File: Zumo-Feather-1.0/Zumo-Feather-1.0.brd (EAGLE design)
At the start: 68.6 x 53.3 mm, 2 parts, among them U1 ARDUINOR3-DIMENSION

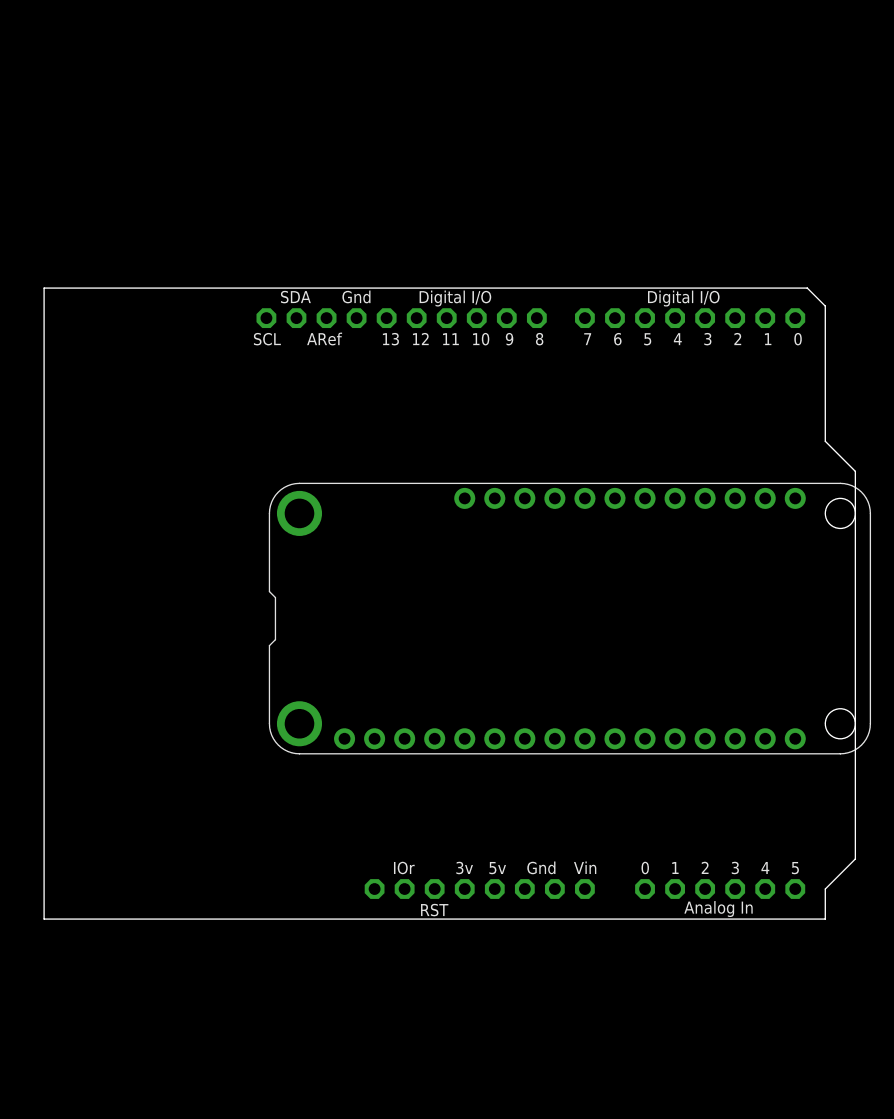
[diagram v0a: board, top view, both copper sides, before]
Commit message: Added CAD and worked on Feather-Zumo Interface board
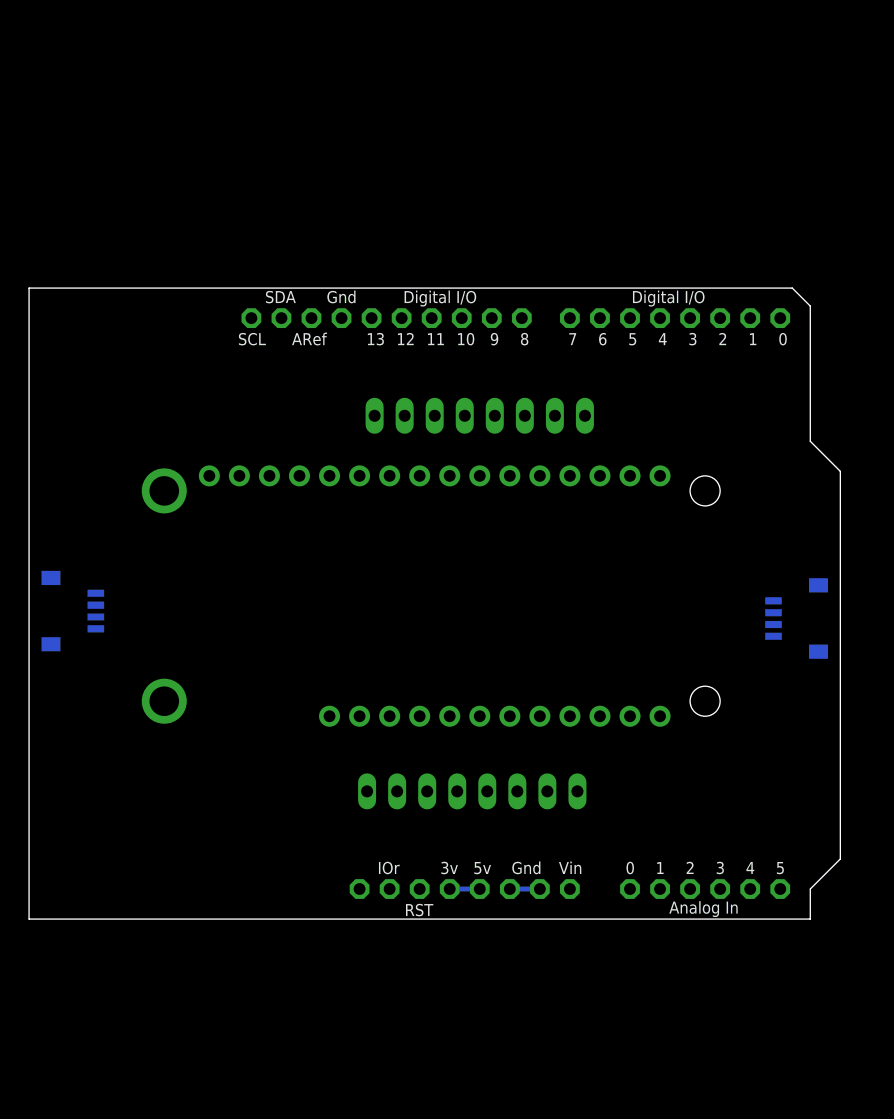
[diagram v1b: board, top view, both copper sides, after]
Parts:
- added J1, J2: (no value), AIMRL:JST_SH_4X1
- added JP1, JP2: (no value), pinhead:1X08
- MS1: value FEATHERWING_NODIM -> BRD-FEATHERWING_NODIM; device adafruit:FEATHERWING_DIM -> AIMRL:FEATHERWING_DIM
- U1: value ARDUINOR3-DIMENSION -> BRD-ARDUINOR3-DIMENSION; device adafruit:ARDUINOR3 -> AIMRL:ARDUINOR3
- moved MS1 27.3 mm to (8.89, 38.7), flipped to the bottom, turned to 180 degrees
- moved U1 1.27 mm to (0.00, 0.00)
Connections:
- net GPIOA0 renamed A0
- net GPIOA2 renamed A2
- net GPIOA3 renamed A3
- net GPIOA4 renamed A4
- net GPIOA5 renamed A5
- net GPIOMISO renamed MISO
- net GPIOMOSI renamed MOSI
- net GPIORX renamed RX
- net GPIOSCK renamed SCK
- net GPIOTX renamed TX
- net USB renamed VUSB
- removed net 5V: U1.5V
- removed net GND1: U1.GND1
- removed net GND2: U1.GND2
- removed net GPIO10: MS1.22
- removed net GPIO11: MS1.23
- removed net GPIO12: MS1.24
- removed net GPIO13: MS1.25
- removed net GPIO5: MS1.19
- removed net GPIO6: MS1.20
- removed net GPIO9: MS1.21
- removed net GPIOA1: MS1.6
- removed net GPIOSCL: MS1.18
- removed net GPIOSDA: MS1.17
- removed net NC: MS1.16
- new net A1: MS1.6, U1.A1
- new net BUZZER: MS1.20, U1.D6
- new net M1DIR: MS1.19, U1.D7
- new net M1PWM: MS1.21, U1.D9
- new net M2DIR: MS1.23, U1.D8
- new net M2PWM: MS1.22, U1.D10
- new net N$1: J1.1, J2.1
- new net N$10: JP2.6
- new net N$11: JP2.7
- new net N$12: JP2.8
- new net N$13: JP1.1
- new net N$14: JP1.2
- new net N$15: JP1.3
- new net N$16: JP1.4
- new net N$17: JP1.5
- new net N$18: JP1.6
- new net N$19: JP1.7
- new net N$2: J1.2, J2.2
- new net N$20: JP1.8
- new net N$3: J1.3, J2.3
- new net N$4: J1.4, J2.4
- new net N$5: JP2.1
- new net N$6: JP2.2
- new net N$7: JP2.3
- new net N$8: JP2.4
- new net N$9: JP2.5
- new net SCL: MS1.18, U1.SCL
- new net SDA: MS1.17, U1.SDA
- new net USER_SW: MS1.24, U1.D12
- new net YELLOW_LED: MS1.25, U1.D13
- net !RESET: now also U1.RESET
- net 3V: now also U1.5V
- net AREF: now also U1.AREF
- net GND: now also U1.GND1, U1.GND2
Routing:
- net GND: track 0.00 -> 2.54 mm
- net 3V: track 0.00 -> 2.54 mm

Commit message: Worked on Zumo board
Swapped pinout around a bunch to make layout easier. Realized power is provided by a 7.5V boost converter, which is not ideal. I will need to jumper VBATT directly from the Zumo Shield or bypass the boost converter.
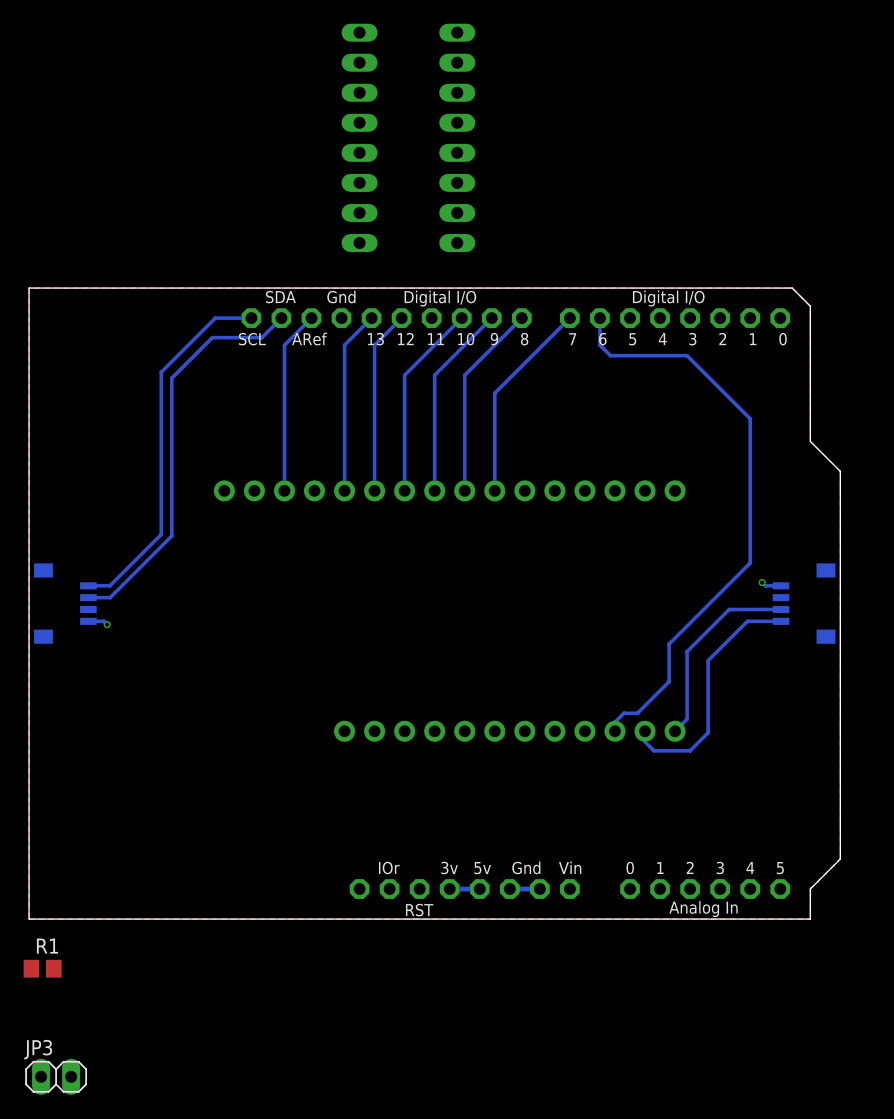
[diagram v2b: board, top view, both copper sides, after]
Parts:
- added JP3: (no value), pinhead:1X02
- added R1: (no value), RLC:R0805
- MS1: value BRD-FEATHERWING_NODIM -> BRD-FEATHERWING_NODIM_NOMNT; device AIMRL:FEATHERWING_DIM -> AIMRL:FEATHERWING_DIM_MNT
- moved JP1 55.3 mm to (36.2, 66.0), turned to 90 degrees
- moved JP2 25.6 mm to (27.9, 66.0), turned to 270 degrees
- moved MS1 1.80 mm to (10.2, 37.5)
- moved J1 1.42 mm to (66.0, 26.7)
- moved J2 0.90 mm to (2.54, 26.7)
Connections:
- removed net A0: MS1.5
- removed net A2: MS1.7
- removed net A3: MS1.8
- removed net A4: MS1.9
- removed net A5: MS1.10
- removed net N$1: J1.1, J2.1
- removed net N$2: J1.2, J2.2
- removed net N$3: J1.3, J2.3
- removed net N$4: J1.4, J2.4
- new net GPIO10: MS1.22
- new net GPIO11: MS1.23
- new net GPIO12: MS1.24
- new net GPIO13: MS1.25
- new net GPIO6: MS1.20
- new net GPIO9: MS1.21
- net 3V: now also J1.2, J2.2
- net A1: no longer MS1.6
- net BUZZER: now also MS1.19; no longer MS1.20
- net GND: now also J1.1, J2.1, JP3.2
- net M1DIR: now also MS1.10; no longer MS1.19
- net M1PWM: now also MS1.8; no longer MS1.21
- net M2DIR: now also MS1.9; no longer MS1.23
- net M2PWM: now also MS1.7; no longer MS1.22
- net SCL: now also J1.4, J2.4
- net SDA: now also J1.3, J2.3
- net USER_SW: now also MS1.6; no longer MS1.24
- net VBAT: now also JP3.1, R1.1
- net VIN: now also R1.2
- net YELLOW_LED: now also MS1.5; no longer MS1.25
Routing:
- net SCL: track 0.00 -> 52.0 mm
- net SDA: track 0.00 -> 50.5 mm
- net BUZZER: track 0.00 -> 49.4 mm
- net M1DIR: track 0.00 -> 17.2 mm
- net M2PWM: track 0.00 -> 16.6 mm
- net M2DIR: track 0.00 -> 16.6 mm
- net M1PWM: track 0.00 -> 16.6 mm
- net AREF: track 0.00 -> 15.6 mm
- net YELLOW_LED: track 0.00 -> 15.6 mm
- net USER_SW: track 0.00 -> 15.6 mm
- net GND: track 2.54 -> 5.95 mm, vias 0 -> 2
- added copper zone on layer 1, net GND

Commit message: Updated schematic
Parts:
- removed R1: (no value), RLC:R0805
- added JP4: (no value), pinhead:1X02
- JP1: device pinhead:1X08 -> pinhead:2X03
- JP2: device pinhead:1X08 -> pinhead:2X02
- moved JP2 32.1 mm to (50.7, 43.4), turned to 0 degrees
- moved JP1 31.6 mm to (58.3, 43.4), turned to 0 degrees
- moved JP3 20.1 mm to (7.24, 6.10), flipped to the bottom, turned to 270 degrees
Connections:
- removed net N$10: JP2.6
- removed net N$11: JP2.7
- removed net N$12: JP2.8
- removed net N$13: JP1.1
- removed net N$14: JP1.2
- removed net N$15: JP1.3
- removed net N$16: JP1.4
- removed net N$17: JP1.5
- removed net N$18: JP1.6
- removed net N$19: JP1.7
- removed net N$20: JP1.8
- removed net N$5: JP2.1
- removed net N$6: JP2.2
- removed net N$7: JP2.3
- removed net N$8: JP2.4
- removed net N$9: JP2.5
- net 3V: now also JP1.2, JP2.4
- net GND: now also JP1.6, JP2.2
- net GPIO13: now also JP1.4
- net MISO: now also JP1.1
- net MOSI: now also JP1.3
- net RX: now also JP2.3
- net SCK: now also JP1.5
- net TX: now also JP2.1
- net VBAT: now also JP4.1; no longer R1.1
- net VIN: now also JP4.2; no longer R1.2
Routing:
- net SCL: track 52.0 -> 0.00 mm
- net SDA: track 50.5 -> 0.00 mm
- net BUZZER: track 49.4 -> 0.00 mm
- net M1DIR: track 17.2 -> 0.00 mm
- net M2PWM: track 16.6 -> 0.00 mm
- net M2DIR: track 16.6 -> 0.00 mm
- net M1PWM: track 16.6 -> 0.00 mm
- net AREF: track 15.6 -> 0.00 mm
- net YELLOW_LED: track 15.6 -> 0.00 mm
- net USER_SW: track 15.6 -> 0.00 mm
- net TX: track 0.00 -> 6.02 mm
- net RX: track 0.00 -> 6.02 mm
- net VIN: track 0.00 -> 3.43 mm
